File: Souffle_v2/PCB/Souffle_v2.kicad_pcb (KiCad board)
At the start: 2 copper layers, 137.2 x 109.2 mm, 81 parts, among them J1 LED, J2 4PIN, J3 OLED, SW1 SW_PUSH, SW10 SW_PUSH, SW11 SW_PUSH, SW12 SW_PUSH, SW13 SW_PUSH, SW14 SW_PUSH, SW15 SW_PUSH, SW16 SW_PUSH, SW17 SW_PUSH, SW18 SW_PUSH, SW19 SW_PUSH, SW2 SW_PUSH, SW20 SW_PUSH, SW21 SW_PUSH, SW22 SW_PUSH, SW23 SW_PUSH, SW24 SW_PUSH, SW25 SW_PUSH, SW25b1 RotaryEncoder_Switch, SW26 SW_PUSH, SW27 SW_PUSH, SW28 SW_PUSH, SW29 SW_PUSH, SW3 SW_PUSH, SW30 SW_PUSH, SW4 SW_PUSH, SW5 SW_PUSH, SW6 SW_PUSH, SW7 SW_PUSH, SW8 SW_PUSH, SW9 SW_PUSH, U1 ProMicro

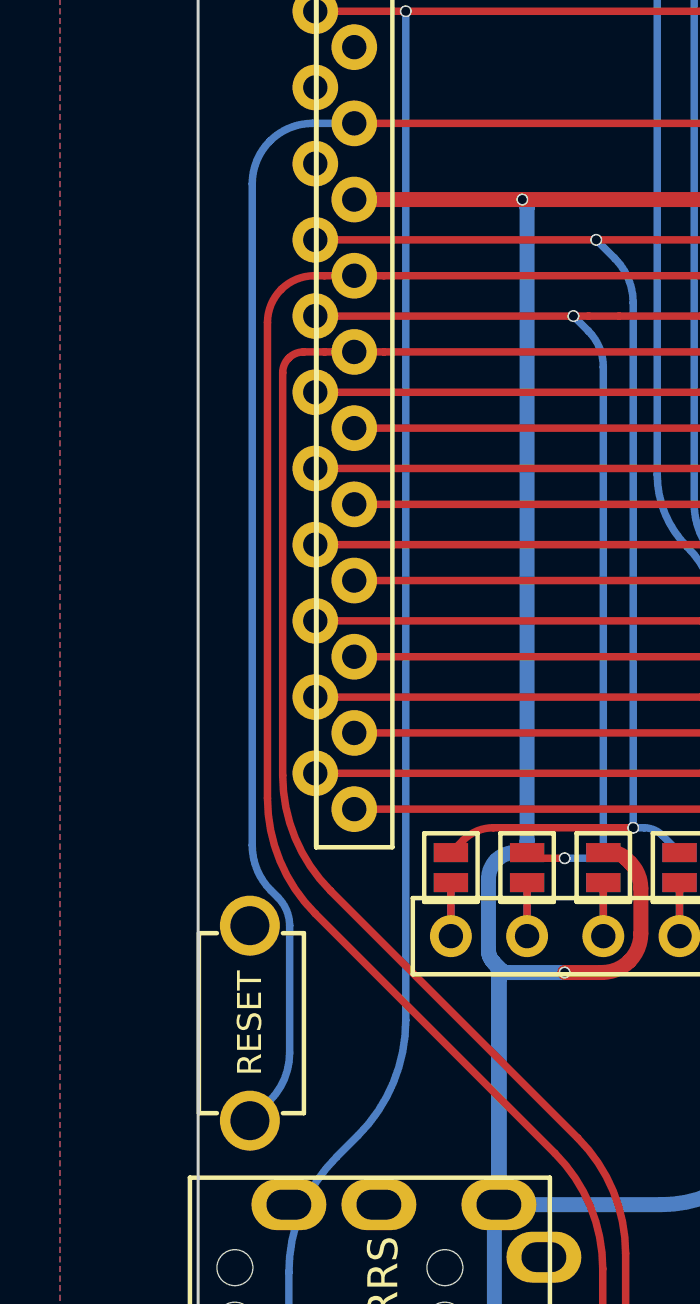
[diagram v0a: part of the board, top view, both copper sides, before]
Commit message: Rotated reset key for shorter track.
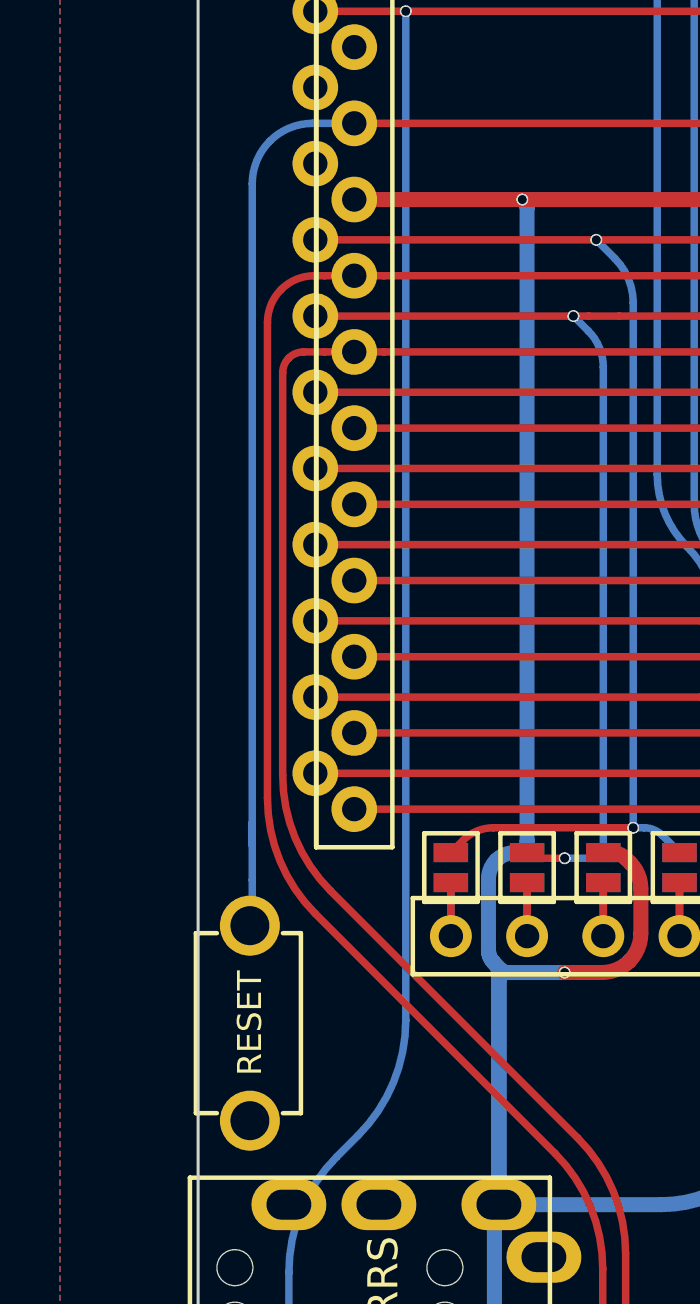
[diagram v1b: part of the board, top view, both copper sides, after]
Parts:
- turned RSW1 to 90 degrees
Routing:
- net RESET: track 51.0 -> 44.5 mm
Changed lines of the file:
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@@
   )
   (footprint "SofleKeyboard-footprint:TACT_SWITCH_TVBP06" (layer "F.Cu")
-    (at 75.634 72.973139 -90)
+    (at 75.634 72.973139 90)
     (property "Sheetfile" "Souffle_v2.kicad_sch")
     (property "Sheetname" "")
@@
       (effects (font (size 1 1) (thickness 0.15)))
     )
-    (fp_text user "RESET" (at 0 0 -90) (layer "F.SilkS")
+    (fp_text user "RESET" (at 0 0 90) (layer "F.SilkS")
       (effects (font (size 0.8 0.8) (thickness 0.15)))
     )
-    (fp_text user "RESET" (at 0 0 -90) (layer "F.SilkS")
+    (fp_text user "RESET" (at 0 0 90) (layer "F.SilkS")
       (effects (font (size 0.8 0.8) (thickness 0.15)))
     )
@@
     (fp_line (start -3 1.7) (end 3 1.7) (layer "F.SilkS") (width 0.15))
     (fp_line (start 3 1.7) (end 3 1.1) (layer "F.SilkS") (width 0.15))
-    (pad "1" thru_hole circle locked (at -3.25 0 270) (size 2 2) (drill 1.3) (layers *.Cu *.Mask)
+    (pad "1" thru_hole circle locked (at -3.25 0 90) (size 2 2) (drill 1.3) (layers *.Cu *.Mask)
       (net 38 "GND") (pinfunction "1") (pintype "passive"))
-    (pad "2" thru_hole circle locked (at 3.25 0 270) (size 2 2) (drill 1.3) (layers *.Cu *.Mask)
+    (pad "2" thru_hole circle locked (at 3.25 0 90) (size 2 2) (drill 1.3) (layers *.Cu *.Mask)
       (net 47 "RESET") (pinfunction "2") (pintype "passive"))
   )
@@
   (via (at 91.968 42.837139) (size 0.4) (drill 0.3) (layers "F.Cu" "B.Cu") (net 47))
   (arc (start 91.897127 42.908011) (mid 91.818625 42.960464) (end 91.726026 42.978884) (width 0.25) (layer "F.Cu") (net 47))
-  (segment (start 75.712 44.992505) (end 75.712 67.045543) (width 0.25) (layer "B.Cu") (net 47))
+  (segment (start 75.634 69.432139) (end 75.712 69.354139) (width 0.25) (layer "B.Cu") (net 47))
   (segment (start 91.984 42.837139) (end 91.968 42.837139) (width 0.25) (layer "B.Cu") (net 47))
-  (segment (start 76.2965 75.560639) (end 75.634 76.223139) (width 0.25) (layer "B.Cu") (net 47))
-  (segment (start 76.959 73.961222) (end 76.959 69.722517) (width 0.25) (layer "B.Cu") (net 47))
   (segment (start 77.725621 42.978884) (end 79.112815 42.978884) (width 0.25) (layer "B.Cu") (net 47))
-  (segment (start 76.3355 68.550806) (end 76.571359 68.786665) (width 0.25) (layer "B.Cu") (net 47))
+  (segment (start 75.712 44.992505) (end 75.712 66.306139) (width 0.25) (layer "B.Cu") (net 47))
+  (segment (start 75.712 69.354139) (end 75.712 68.200139) (width 0.25) (layer "B.Cu") (net 47))
+  (segment (start 75.634 69.723139) (end 75.634 69.432139) (width 0.25) (layer "B.Cu") (net 47))
+  (segment (start 75.712 66.306139) (end 75.712 67.045543) (width 0.25) (layer "B.Cu") (net 47))
+  (segment (start 75.712 66.306139) (end 75.712 68.200139) (width 0.25) (layer "B.Cu") (net 47))
   (segment (start 92.011313 42.825825) (end 93.054 41.783139) (width 0.25) (layer "B.Cu") (net 47))
-  (arc (start 76.571359 68.786665) (mid 76.858256 69.216038) (end 76.959 69.722517) (width 0.25) (layer "B.Cu") (net 47))
   (arc (start 76.301776 43.56866) (mid 75.865277 44.221925) (end 75.712 44.992505) (width 0.25) (layer "B.Cu") (net 47))
   (arc (start 92.011313 42.825825) (mid 91.998781 42.834198) (end 91.984 42.837139) (width 0.25) (layer "B.Cu") (net 47))
-  (arc (start 75.712 67.045543) (mid 75.874042 67.860185) (end 76.3355 68.550806) (width 0.25) (layer "B.Cu") (net 47))
-  (arc (start 76.959 73.961222) (mid 76.786821 74.82682) (end 76.2965 75.560639) (width 0.25) (layer "B.Cu") (net 47))
   (arc (start 77.725621 42.978884) (mid 76.955041 43.132161) (end 76.301776 43.56866) (width 0.25) (layer "B.Cu") (net 47))
   (segment (start 98.934 68.580139) (end 98.934 78.213764) (width 0.25) (layer "F.Cu") (net 48))

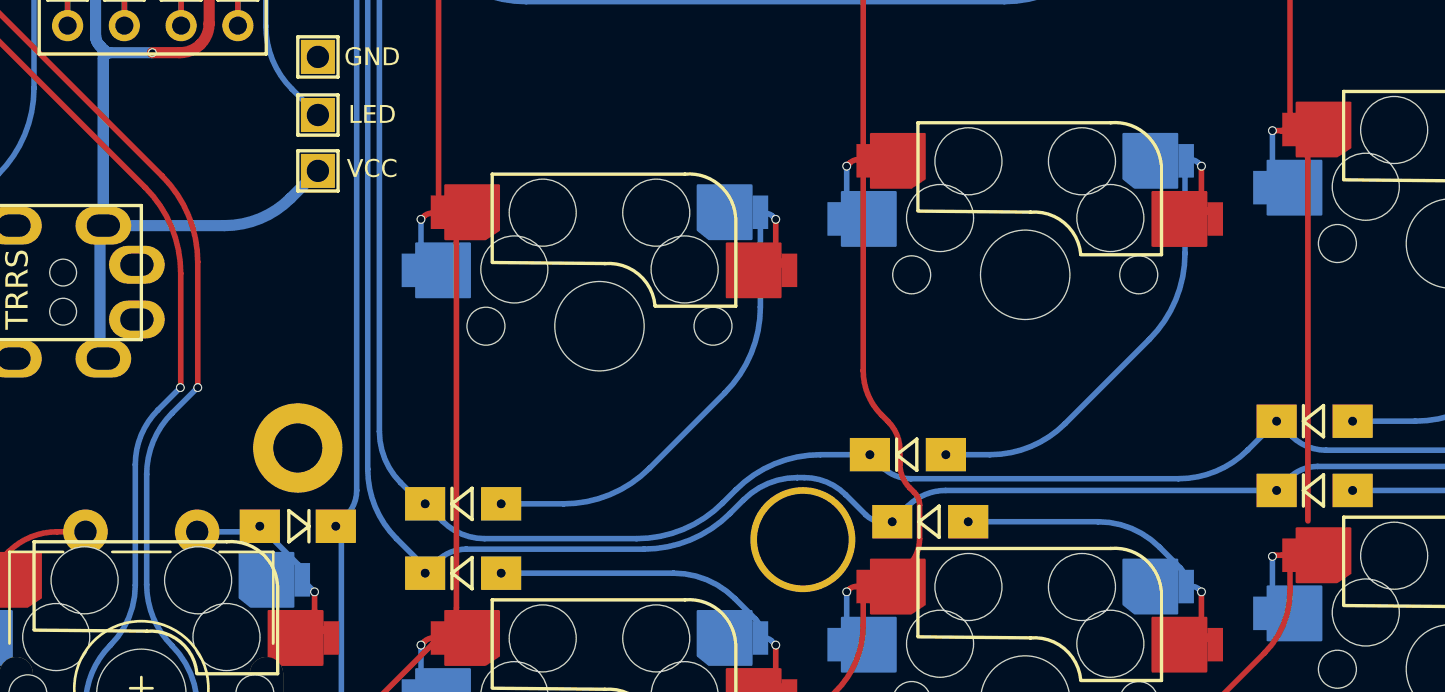
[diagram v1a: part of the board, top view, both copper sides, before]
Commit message: Fix track for column 2. Was unconnected.
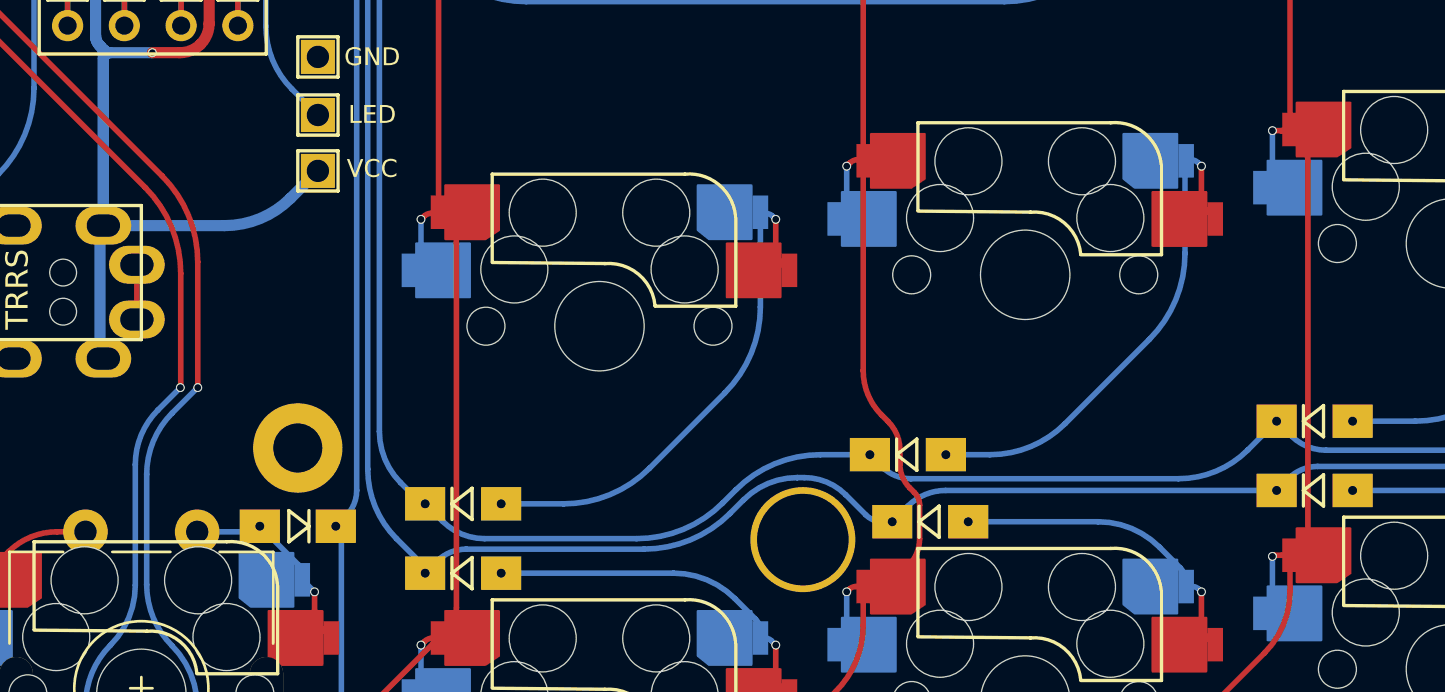
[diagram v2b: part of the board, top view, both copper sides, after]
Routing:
- net unconnected-(J2-Pad4): track 0.00 -> 2.45 mm
- net col3: track 188.8 -> 190.6 mm
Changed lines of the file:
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@@
   (arc (start 78.527792 77.429345) (mid 77.348213 79.194711) (end 76.934 81.277102) (width 0.25) (layer "B.Cu") (net 39))
   (arc (start 80.83 72.873175) (mid 80.415786 74.955565) (end 79.236207 76.720931) (width 0.25) (layer "B.Cu") (net 39))
+  (segment (start 85.434 80.773139) (end 85.434 83.223139) (width 0.25) (layer "F.Cu") (net 40))
   (segment (start 82.334 68.287519) (end 82.334 70.073139) (width 0.25) (layer "F.Cu") (net 41))
   (segment (start 82.334 68.418518) (end 82.334 70.073139) (width 0.25) (layer "B.Cu") (net 41))
@@
   (arc (start 117.1965 58.712891) (mid 117.123405 59.080362) (end 116.91525 59.391889) (width 0.25) (layer "B.Cu") (net 49))
   (segment (start 137.280603 36.829742) (end 137.434 36.983139) (width 0.25) (layer "F.Cu") (net 50))
-  (segment (start 137.834 76.138824) (end 137.834 92.235639) (width 0.25) (layer "F.Cu") (net 50))
   (segment (start 113.254798 105.75234) (end 106.833149 112.173989) (width 0.25) (layer "F.Cu") (net 50))
   (segment (start 136.2715 55.698139) (end 136.2465 55.723139) (width 0.25) (layer "F.Cu") (net 50))
   (segment (start 136.2715 93.798139) (end 136.2465 93.823139) (width 0.25) (layer "F.Cu") (net 50))
-  (segment (start 137.434 75.173139) (end 137.312423 75.051562) (width 0.25) (layer "F.Cu") (net 50))
+  (segment (start 137.834 92.973139) (end 137.034 93.773139) (width 0.25) (layer "F.Cu") (net 50))
   (segment (start 137.834 54.307453) (end 137.834 37.948824) (width 0.25) (layer "F.Cu") (net 50))
   (segment (start 136.331855 55.673139) (end 136.66525 55.673139) (width 0.25) (layer "F.Cu") (net 50))
+  (segment (start 137.834 76.138824) (end 137.834 92.973139) (width 0.25) (layer "F.Cu") (net 50))
   (segment (start 136.2465 74.773139) (end 136.64025 74.773139) (width 0.25) (layer "F.Cu") (net 50))
   (segment (start 105.239357 118.655348) (end 105.239357 116.021745) (width 0.25) (layer "F.Cu") (net 50))
@@
   (segment (start 137.034 94.141889) (end 137.034 95.388764) (width 0.25) (layer "F.Cu") (net 50))
   (segment (start 137.294745 55.412393) (end 137.434 55.273139) (width 0.25) (layer "F.Cu") (net 50))
+  (segment (start 137.312423 75.051562) (end 137.434 75.173139) (width 0.25) (layer "F.Cu") (net 50))
   (segment (start 136.2915 36.628139) (end 136.2465 36.673139) (width 0.25) (layer "F.Cu") (net 50))
   (segment (start 91.862375 60.722763) (end 91.898496 60.686643) (width 0.25) (layer "F.Cu") (net 50))
@@
   (via (at 136.2465 93.823139) (size 0.4) (drill 0.3) (layers "F.Cu" "B.Cu") (net 50))
   (arc (start 137.312423 75.051562) (mid 137.004027 74.845498) (end 136.64025 74.773139) (width 0.25) (layer "F.Cu") (net 50))
-  (arc (start 137.434 75.173139) (mid 137.730043 75.616199) (end 137.834 76.138824) (width 0.25) (layer "F.Cu") (net 50))
   (arc (start 105.239357 118.655348) (mid 105.188081 118.779138) (end 105.064291 118.830414) (width 0.25) (layer "F.Cu") (net 50))
   (arc (start 137.294745 55.412393) (mid 137.101765 55.701208) (end 137.034 56.041889) (width 0.25) (layer "F.Cu") (net 50))
@@
   (arc (start 91.862375 60.722763) (mid 91.822366 60.749496) (end 91.775172 60.758884) (width 0.25) (layer "F.Cu") (net 50))
   (arc (start 137.034 95.388764) (mid 136.737094 96.881406) (end 135.89158 98.146808) (width 0.25) (layer "F.Cu") (net 50))
+  (arc (start 137.434 75.173139) (mid 137.730043 75.616199) (end 137.834 76.138824) (width 0.25) (layer "F.Cu") (net 50))
   (arc (start 137.434 36.983139) (mid 137.730043 37.426199) (end 137.834 37.948824) (width 0.25) (layer "F.Cu") (net 50))
   (arc (start 136.66525 55.673139) (mid 137.00593 55.605373) (end 137.294745 55.412393) (width 0.25) (layer "F.Cu") (net 50))
